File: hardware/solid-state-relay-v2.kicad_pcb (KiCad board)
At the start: 2 copper layers, 19 x 33.4 mm, 22 parts, among them P1 CON-SENSOR2, P2 TST, P3 TST, P5 BOOT, Q1 2N7002P, U1 XMC110024, U2 DRILL, U3 DRILL

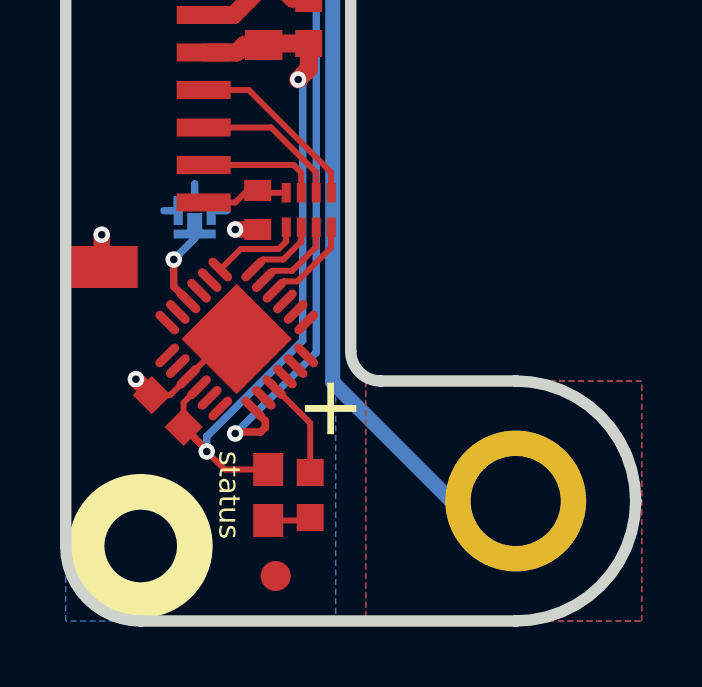
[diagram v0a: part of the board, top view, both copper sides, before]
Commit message: Change capacitor footprint(s) to C0402F
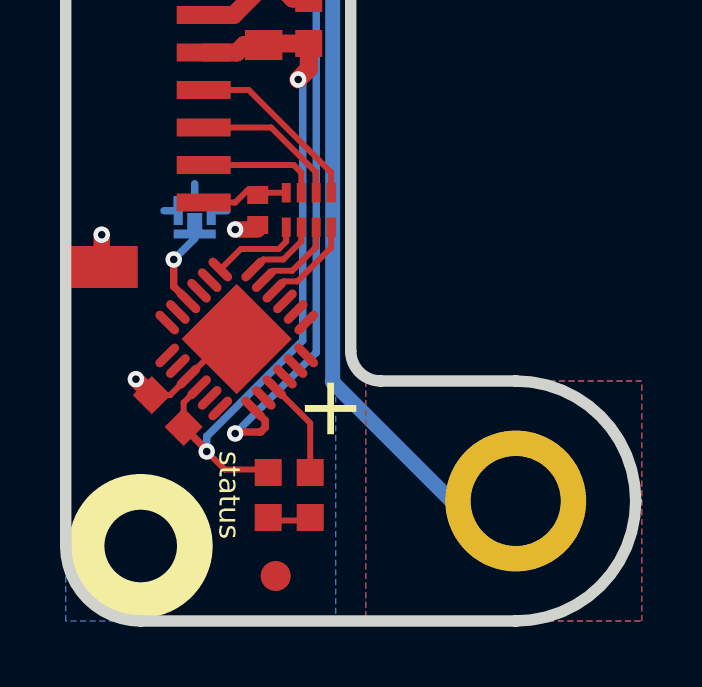
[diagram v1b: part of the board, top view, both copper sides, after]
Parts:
- C1: footprint kicad-libraries:C0402E -> kicad-libraries:C0402F
- D1: footprint kicad-libraries:D0603E -> kicad-libraries:D0603F
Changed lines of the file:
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@@
-(kicad_pcb (version 4) (host pcbnew 4.0.7-e2-6376~58~ubuntu17.04.1)
+(kicad_pcb (version 4) (host pcbnew 4.0.2+dfsg1-stable)
   (general
     (links 40)
     (no_connects 0)
-    (area 97.544999 48.644999 282.27147 165.489573)
+    (area 98.209499 49.309499 117.590501 83.090501)
     (thickness 1.6002)
     (drawings 19)
@@
       (clearance 0.65024))
   )
-  (module kicad-libraries:C0402E (layer Vorderseite)
-    (at 104.8 69.2 270)
-    (attr smd)
-    (fp_text reference C1 (at 0 0.125 270) (layer F.Fab)
-      (effects (font (size 0.2 0.2) (thickness 0.05)))
-    )
-    (fp_text value 220pF (at 0 -0.275 270) (layer F.Fab)
-      (effects (font (size 0.2 0.2) (thickness 0.05)))
-    )
-    (fp_line (start -0.8509 -0.44958) (end 0.8509 -0.44958) (layer F.Fab) (width 0.001))
-    (fp_line (start 0.8509 -0.44958) (end 0.8509 0.44958) (layer F.Fab) (width 0.001))
-    (fp_line (start 0.8509 0.44958) (end -0.8509 0.44958) (layer F.Fab) (width 0.001))
-    (fp_line (start -0.8509 0.44958) (end -0.8509 -0.44958) (layer F.Fab) (width 0.001))
-    (pad 1 smd rect (at -0.65 0 270) (size 0.7 0.9) (layers Vorderseite F.Paste F.Mask)
-      (net 9 "Net-(C1-Pad1)"))
-    (pad 2 smd rect (at 0.65 0 270) (size 0.7 0.9) (layers Vorderseite F.Paste F.Mask)
-      (net 2 GND))
-    (model Capacitors_SMD/C_0402.wrl
-      (at (xyz 0 0 0))
-      (scale (xyz 1 1 1))
-      (rotate (xyz 0 0 0))
-    )
-  )
   (module kicad-libraries:C0805 (layer Vorderseite)
     (at 105 62.7 90)
@@
     )
   )
-  (module kicad-libraries:D0603E (layer Vorderseite)
-    (at 105.15 78.7 270)
-    (attr smd)
-    (fp_text reference D1 (at 0.85 0.45 270) (layer F.Fab)
-      (effects (font (size 0.2 0.2) (thickness 0.05)))
-    )
-    (fp_text value blue (at 0.85 -0.5 270) (layer F.Fab)
-      (effects (font (size 0.2 0.2) (thickness 0.05)))
-    )
-    (fp_line (start 0.2 -0.4) (end 0.2 0.4) (layer F.Fab) (width 0.05))
-    (fp_line (start 0.2 0) (end -0.2 -0.4) (layer F.Fab) (width 0.05))
-    (fp_line (start -0.2 -0.4) (end -0.2 0.4) (layer F.Fab) (width 0.05))
-    (fp_line (start -0.2 0.4) (end 0.2 0) (layer F.Fab) (width 0.05))
-    (fp_line (start -0.889 -0.254) (end -0.889 0.254) (layer F.Fab) (width 0.05))
-    (fp_line (start -1.143 0) (end -0.635 0) (layer F.Fab) (width 0.05))
-    (fp_line (start -1.45034 -0.65024) (end 1.45034 -0.65024) (layer F.Fab) (width 0.001))
-    (fp_line (start 1.45034 -0.65024) (end 1.45034 0.65024) (layer F.Fab) (width 0.001))
-    (fp_line (start 1.45034 0.65024) (end -1.45034 0.65024) (layer F.Fab) (width 0.001))
-    (fp_line (start -1.45034 0.65024) (end -1.45034 -0.65024) (layer F.Fab) (width 0.001))
-    (pad 1 smd rect (at -0.8501 0 270) (size 1.1 1) (layers Vorderseite F.Paste F.Mask)
-      (net 3 VCC))
-    (pad 2 smd rect (at 0.8501 0 270) (size 1.1 1) (layers Vorderseite F.Paste F.Mask)
-      (net 10 "Net-(D1-Pad2)"))
-    (model LED_SMD/D_0603_blue.wrl
-      (at (xyz 0 0 0))
-      (scale (xyz 1 1 1))
-      (rotate (xyz 90 180 0))
-    )
-  )
   (module kicad-libraries:CON-SENSOR2 (layer Vorderseite)
     (at 98.4 65.2 270)
@@
       (xy 2.3114 -1.41732) (xy 2.3114 -1.67132) (xy 2.3114 -1.67132)) (layer B.SilkS) (width 0.00254))
   )
+  (module kicad-libraries:C0402F (layer Vorderseite)
+    (at 104.8 69.2 270)
+    (fp_text reference C1 (at 0.1 0.15 270) (layer F.Fab)
+      (effects (font (size 0.2 0.2) (thickness 0.05)))
+    )
+    (fp_text value 220pF (at 0 -0.15 270) (layer F.Fab)
+      (effects (font (size 0.2 0.2) (thickness 0.05)))
+    )
+    (fp_line (start -0.9 -0.45) (end 0.9 -0.45) (layer F.Fab) (width 0.025))
+    (fp_line (start 0.9 -0.45) (end 0.9 0.45) (layer F.Fab) (width 0.025))
+    (fp_line (start 0.9 0.45) (end -0.9 0.45) (layer F.Fab) (width 0.025))
+    (fp_line (start -0.9 0.45) (end -0.9 -0.45) (layer F.Fab) (width 0.025))
+    (pad 2 smd rect (at 0.5 0 270) (size 0.6 0.7) (layers Vorderseite F.Paste F.Mask)
+      (net 2 GND))
+    (pad 1 smd rect (at -0.5 0 270) (size 0.6 0.7) (layers Vorderseite F.Paste F.Mask)
+      (net 9 "Net-(C1-Pad1)"))
+    (model Capacitors_SMD/C_0402.wrl
+      (at (xyz 0 0 0))
+      (scale (xyz 1 1 1))
+      (rotate (xyz 0 0 0))
+    )
+  )
+  (module kicad-libraries:D0603F (layer Vorderseite)
+    (at 105.15 78.7 270)
+    (attr smd)
+    (fp_text reference D1 (at -0.775 0.45 270) (layer F.Fab)
+      (effects (font (size 0.2 0.2) (thickness 0.05)))
+    )
+    (fp_text value blue (at 0.75 0.45 270) (layer F.Fab)
+      (effects (font (size 0.2 0.2) (thickness 0.05)))
+    )
+    (fp_line (start -0.75 -0.3) (end -0.75 0.3) (layer F.Fab) (width 0.05))
+    (fp_line (start -1.05 0) (end -0.45 0) (layer F.Fab) (width 0.05))
+    (fp_line (start 0.45 0) (end 1.05 0) (layer F.Fab) (width 0.05))
+    (fp_line (start 0 -0.3) (end 0 0.3) (layer F.Fab) (width 0.05))
+    (fp_line (start -0.3 -0.3) (end -0.3 0.3) (layer F.Fab) (width 0.05))
+    (fp_line (start -0.3 0.3) (end 0 0) (layer F.Fab) (width 0.05))
+    (fp_line (start 0 0) (end -0.3 -0.3) (layer F.Fab) (width 0.05))
+    (fp_line (start -1.45034 -0.65024) (end 1.45034 -0.65024) (layer F.Fab) (width 0.001))
+    (fp_line (start 1.45034 -0.65024) (end 1.45034 0.65024) (layer F.Fab) (width 0.001))
+    (fp_line (start 1.45034 0.65024) (end -1.45034 0.65024) (layer F.Fab) (width 0.001))
+    (fp_line (start -1.45034 0.65024) (end -1.45034 -0.65024) (layer F.Fab) (width 0.001))
+    (pad 1 smd rect (at -0.75 0 270) (size 0.9 0.9) (layers Vorderseite F.Paste F.Mask)
+      (net 3 VCC))
+    (pad 2 smd rect (at 0.75 0 270) (size 0.9 0.9) (layers Vorderseite F.Paste F.Mask)
+      (net 10 "Net-(D1-Pad2)"))
+    (model LED_SMD/D_0603_blue.wrl
+      (at (xyz 0 0 0))
+      (scale (xyz 1 1 1))
+      (rotate (xyz -90 0 0))
+    )
+  )
   (gr_text status (at 103.85 78.7 270) (layer F.SilkS)

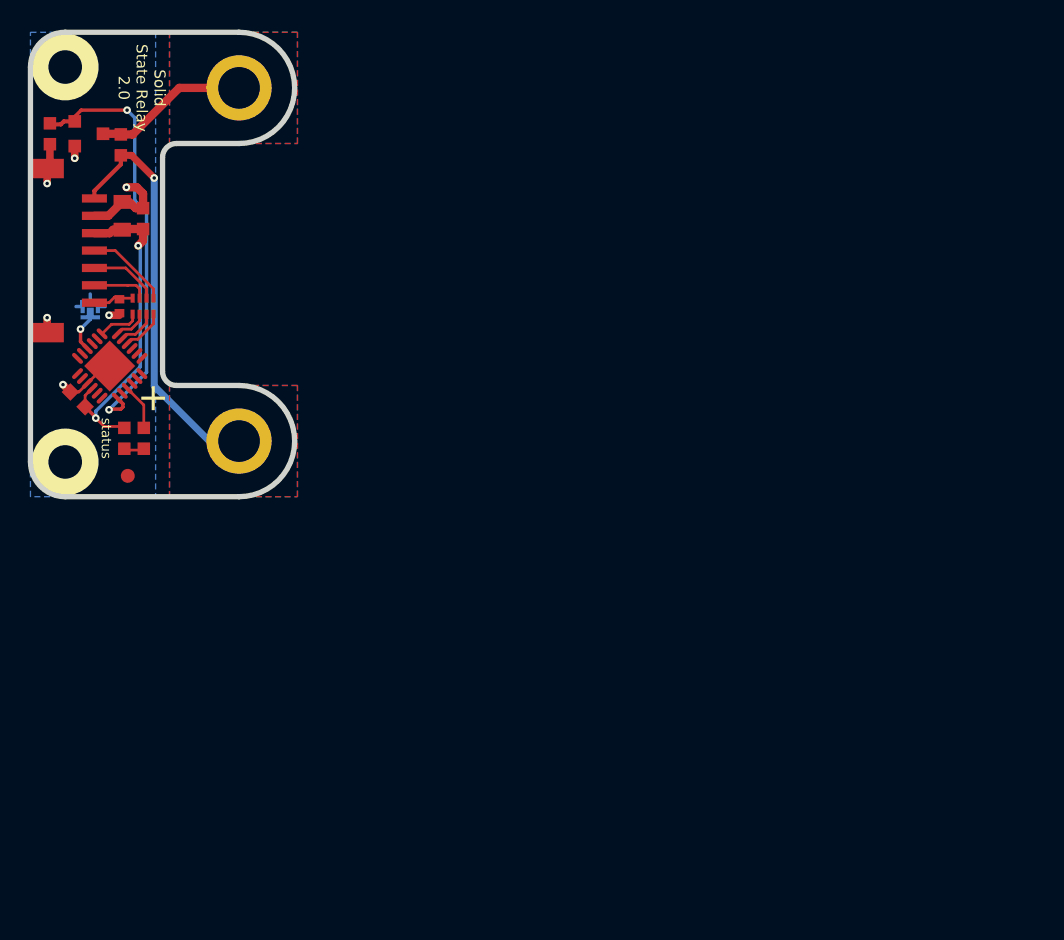
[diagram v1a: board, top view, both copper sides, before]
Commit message: New standart layout. Switched to Kicad 6
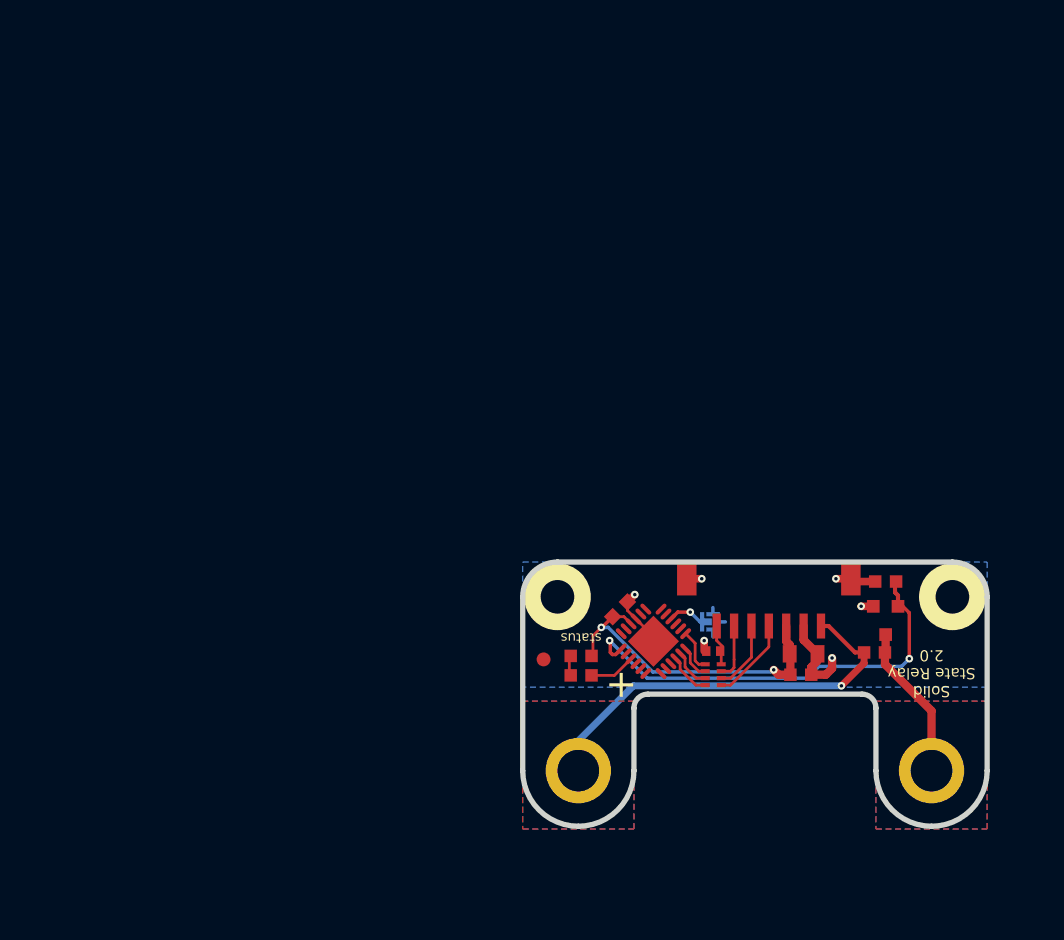
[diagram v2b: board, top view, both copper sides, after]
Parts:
- moved U2 74.3 mm to (164.7, 90.1), turned to -90 degrees
- moved VAL 72.5 mm to (164.4, 95.2), turned to 0 degrees
- moved P2 69.9 mm to (163.2, 102.6), turned to -90 degrees
- moved R1 68.2 mm to (159.9, 89.0), turned to 180 degrees
- moved Q1 67.1 mm to (159.9, 91.8), turned to 0 degrees
- moved R2 65.3 mm to (159.1, 94.1), turned to 0 degrees
- moved VAL 64.8 mm to (158.2, 92.1), turned to 0 degrees
- moved C2 58.3 mm to (154.0, 94.2), turned to 0 degrees
- moved P1 57.6 mm to (151.5, 87.6), turned to 180 degrees
- moved C3 57.6 mm to (153.8, 95.7), turned to 0 degrees
- moved G*** 55.9 mm to (152.0, 93.1), turned to 180 degrees
- moved P5 49.9 mm to (147.2, 91.9), turned to 180 degrees
- moved C1 49.4 mm to (147.5, 94.0), turned to 180 degrees
- moved RP1 48.8 mm to (147.5, 95.7), turned to 90 degrees
- moved U1 43.8 mm to (143.2, 93.3), turned to -135 degrees
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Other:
- board size 19 x 33.4 mm -> 33.4 x 19 mm
- net class Default removed

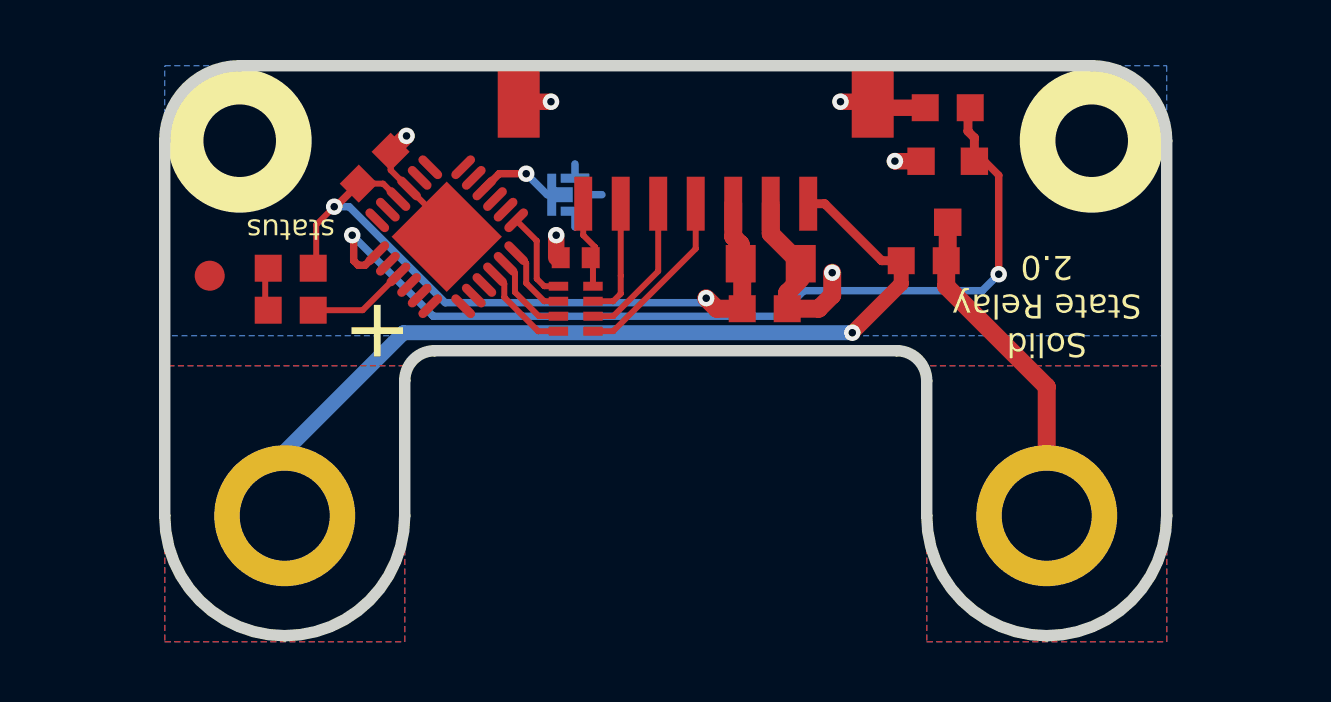
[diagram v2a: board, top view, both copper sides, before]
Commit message: Hardware 2.1: Made Pcb bigger to fit on the 40mm grid. Data Cleanup
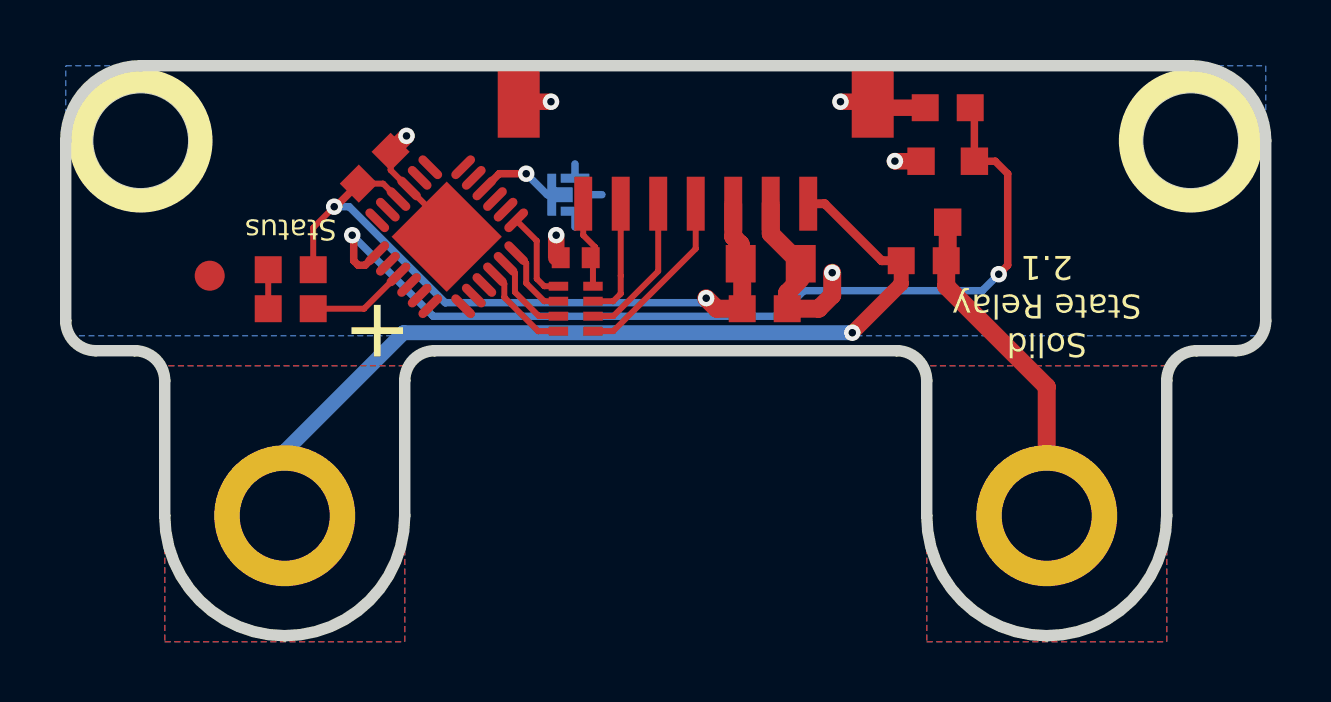
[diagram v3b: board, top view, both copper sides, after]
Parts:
- moved U2 3.30 mm to (168.0, 90.1)
- moved U3 3.30 mm to (133.0, 90.1)
- moved D1 0.05 mm to (138.0, 94.4)
- renumbered P3 to P2, P2 to P3
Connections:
- U1 pad 11: Net-(U1-Pad11) -> unconnected-(U1-Pad11)
- U1 pad 12: Net-(U1-Pad12) -> unconnected-(U1-Pad12)
- U1 pad 14: Net-(U1-Pad14) -> unconnected-(U1-Pad14)
- U1 pad 16: Net-(U1-Pad16) -> unconnected-(U1-Pad16)
- U1 pad 17: Net-(U1-Pad17) -> unconnected-(U1-Pad17)
- U1 pad 18: Net-(U1-Pad18) -> unconnected-(U1-Pad18)
- U1 pad 19: Net-(U1-Pad19) -> unconnected-(U1-Pad19)
- U1 pad 2: Net-(U1-Pad2) -> unconnected-(U1-Pad2)
- U1 pad 20: Net-(U1-Pad20) -> unconnected-(U1-Pad20)
- U1 pad 21: Net-(U1-Pad21) -> unconnected-(U1-Pad21)
- U1 pad 3: Net-(U1-Pad3) -> unconnected-(U1-Pad3)
- U1 pad 5: Net-(U1-Pad5) -> unconnected-(U1-Pad5)
- U1 pad 6: Net-(U1-Pad6) -> unconnected-(U1-Pad6)
- U1 pad 7: Net-(U1-Pad7) -> unconnected-(U1-Pad7)
- U1 pad 8: Net-(U1-Pad8) -> unconnected-(U1-Pad8)
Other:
- board size 33.4 x 19 mm -> 40 x 19 mm
- board text added: "Copyright Tinkerforge GmbH 2023. This documentation describes Open Hardware and is licensed under the CERN OHL v. 1.1. You may redistribute and modify this documentation under the terms of the CERN OHL v.1.1. (http://ohwr.org/cernohl). This documentation is distributed WITHOUT ANY EXPRESS OR IMPLIED WARRANTY, INCLUDING OF MERCHANTABILITY, SATISFACTORY QUALITY AND FITNESS FOR A PARTICULAR PURPOSE.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"
- board text added: "Solid State Relay 2.1"
- board text added: "Status"
- board text removed: "Copyright Tinkerforge GmbH 2014. This documentation describes Open Hardware and is licensed under the CERN OHL v. 1.1. You may redistribute and modify this documentation under the terms of the CERN OHL v.1.1. (http://ohwr.org/cernohl). This documentation is distributed WITHOUT ANY EXPRESS OR IMPLIED WARRANTY, INCLUDING OF MERCHANTABILITY, SATISFACTORY QUALITY AND FITNESS FOR A PARTICULAR PURPOSE.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"
- board text removed: "Solid State Relay 2.0"
- board text removed: "status"
